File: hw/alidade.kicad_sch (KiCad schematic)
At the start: 0 parts

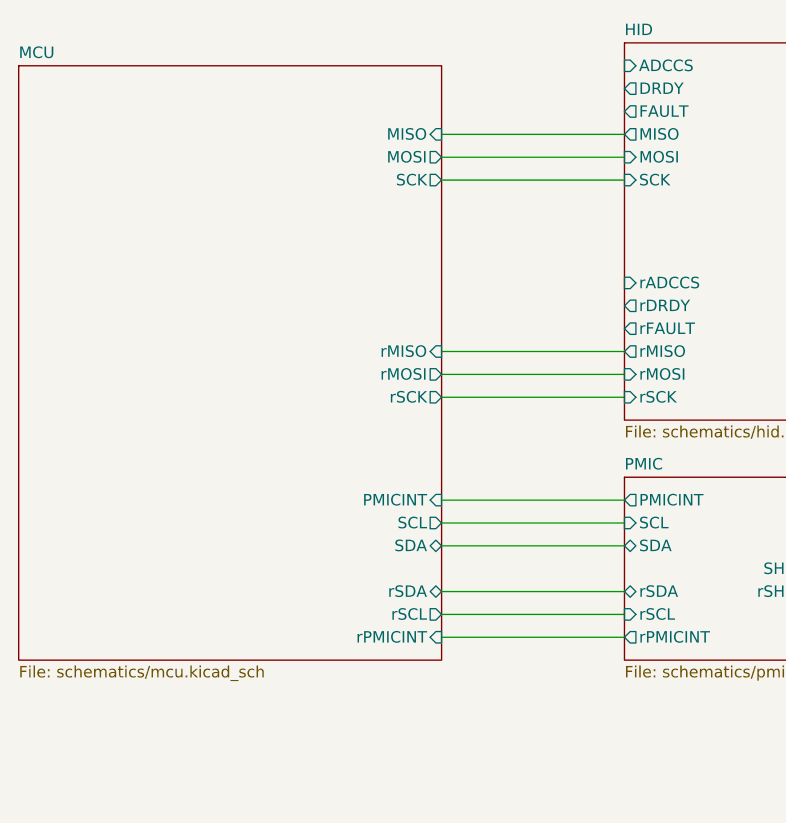
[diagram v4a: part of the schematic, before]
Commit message: Solve erc errors
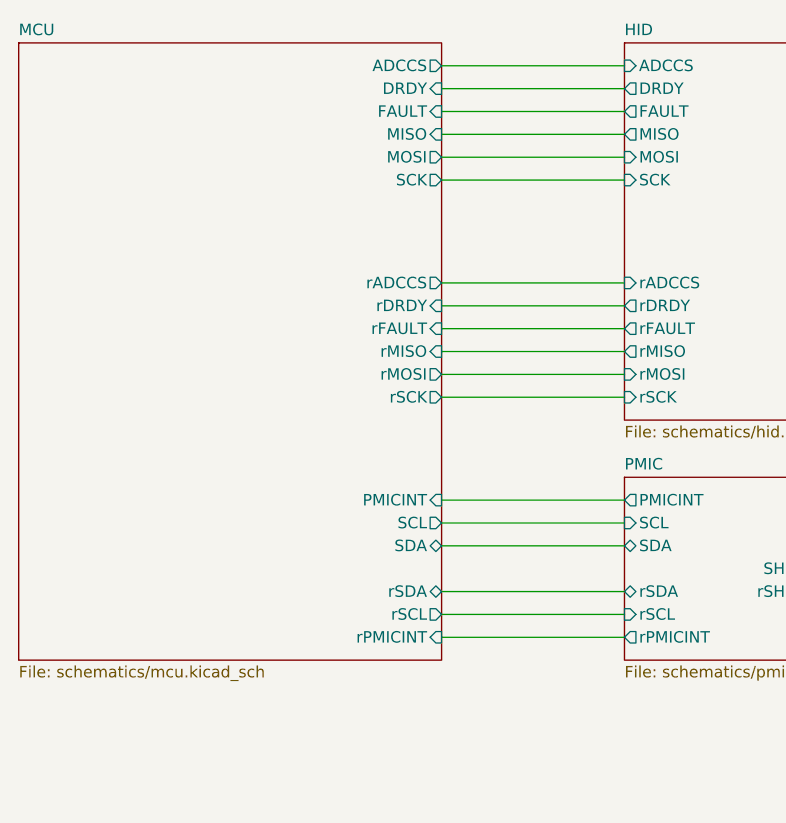
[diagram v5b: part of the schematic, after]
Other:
- sheet MCU ports: added ADCCS, DRDY, FAULT, rADCCS, rDRDY, rFAULT; removed none
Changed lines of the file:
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@@
+	(wire
+		(pts
+			(xy 173.99 154.94) (xy 194.31 154.94)
+		)
+		(stroke
+			(width 0)
+			(type default)
+		)
+	)
 	(wire
 		(pts
@@
 	(wire
 		(pts
+			(xy 173.99 160.02) (xy 194.31 160.02)
+		)
+		(stroke
+			(width 0)
+			(type default)
+		)
+	)
+	(wire
+		(pts
 			(xy 173.99 194.31) (xy 194.31 194.31)
 		)
@@
 	(wire
 		(pts
+			(xy 173.99 157.48) (xy 194.31 157.48)
+		)
+		(stroke
+			(width 0)
+			(type default)
+		)
+	)
+	(wire
+		(pts
 			(xy 237.49 186.69) (xy 237.49 193.04)
 		)
@@
 		(pts
 			(xy 173.99 184.15) (xy 194.31 184.15)
+		)
+		(stroke
+			(width 0)
+			(type default)
+		)
+	)
+	(wire
+		(pts
+			(xy 173.99 133.35) (xy 194.31 133.35)
+		)
+		(stroke
+			(width 0)
+			(type default)
+		)
+	)
+	(wire
+		(pts
+			(xy 173.99 130.81) (xy 194.31 130.81)
+		)
+		(stroke
+			(width 0)
+			(type default)
+		)
+	)
+	(wire
+		(pts
+			(xy 173.99 135.89) (xy 194.31 135.89)
 		)
 		(stroke
@@
 	)
 	(sheet
-		(at 127 130.81)
-		(size 46.99 66.04)
+		(at 127 128.27)
+		(size 46.99 68.58)
 		(exclude_from_sim no)
 		(in_bom yes)
@@
 		)
 		(property "Sheetname" "MCU"
-			(at 127 130.0984 0)
+			(at 127 127.5584 0)
 			(effects
 				(font
@@
 			(effects
 				(font
+					(size 1.27 1.27)
+				)
+				(justify right)
+			)
+		)
+		(pin "ADCCS" output
+			(at 173.99 130.81 0)
+			(effects
+				(font
+					(size 1.27 1.27)
+				)
+				(justify right)
+			)
+		)
+		(pin "DRDY" input
+			(at 173.99 133.35 0)
+			(effects
+				(font
+					(size 1.27 1.27)
+				)
+				(justify right)
+			)
+		)
+		(pin "FAULT" input
+			(at 173.99 135.89 0)
+			(effects
+				(font
+					(size 1.27 1.27)
+				)
+				(justify right)
+			)
+		)
+		(pin "rADCCS" output
+			(at 173.99 154.94 0)
+			(effects
+				(font
+					(size 1.27 1.27)
+				)
+				(justify right)
+			)
+		)
+		(pin "rDRDY" input
+			(at 173.99 157.48 0)
+			(effects
+				(font
+					(size 1.27 1.27)
+				)
+				(justify right)
+			)
+		)
+		(pin "rFAULT" input
+			(at 173.99 160.02 0)
+			(effects
+				(font
